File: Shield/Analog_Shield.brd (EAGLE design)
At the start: 115.2 x 89.7 mm, 74 parts, among them IC1 7805TV, IC2 LM340MP-05

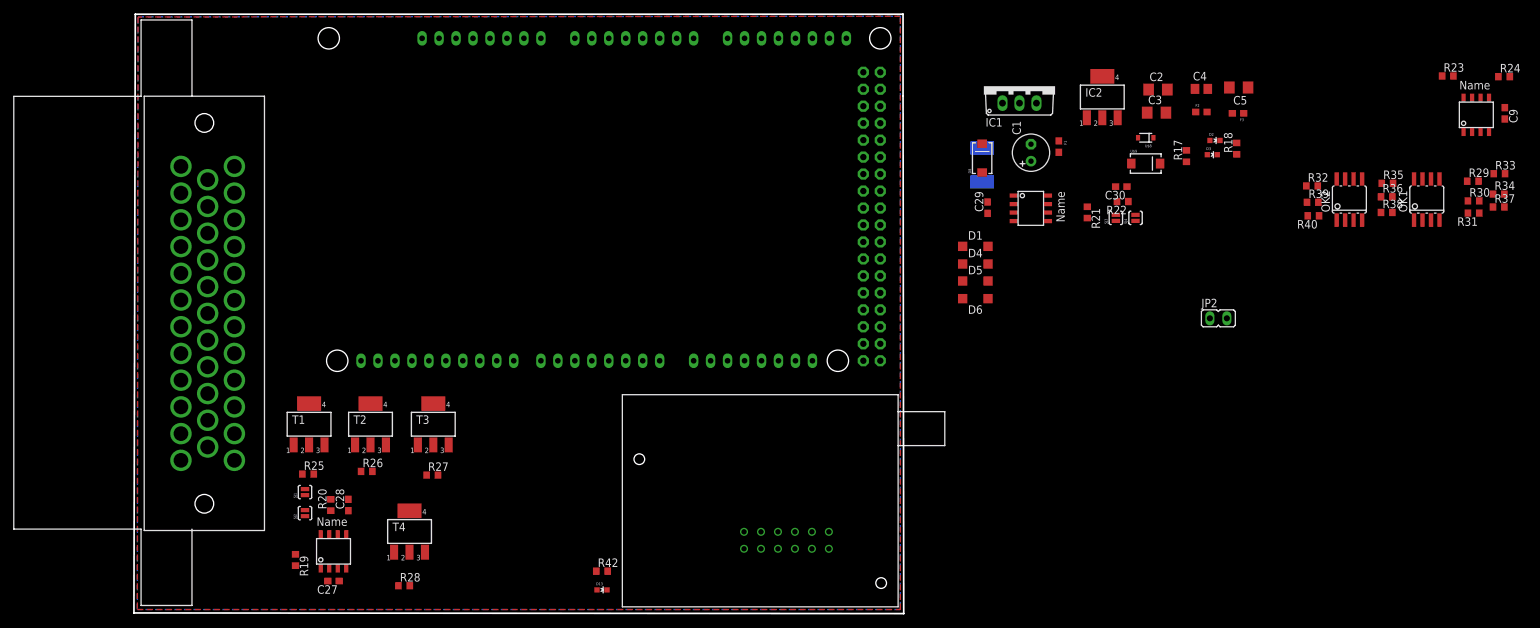
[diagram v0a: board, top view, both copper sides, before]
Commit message: Added analog shield, flipped Due on Dued board, fixed miniwifi footprint
Added an analog shield that will be used for all analog input instead of placing it on the main DueD board. Also, now all boards will be two layer instead of four.

Flipped over the Due on the DueD board. Now the DueD board is to have pins that stick up for the Due to
mate to.

Drastically improved the accuracy of the miniwifi layout.
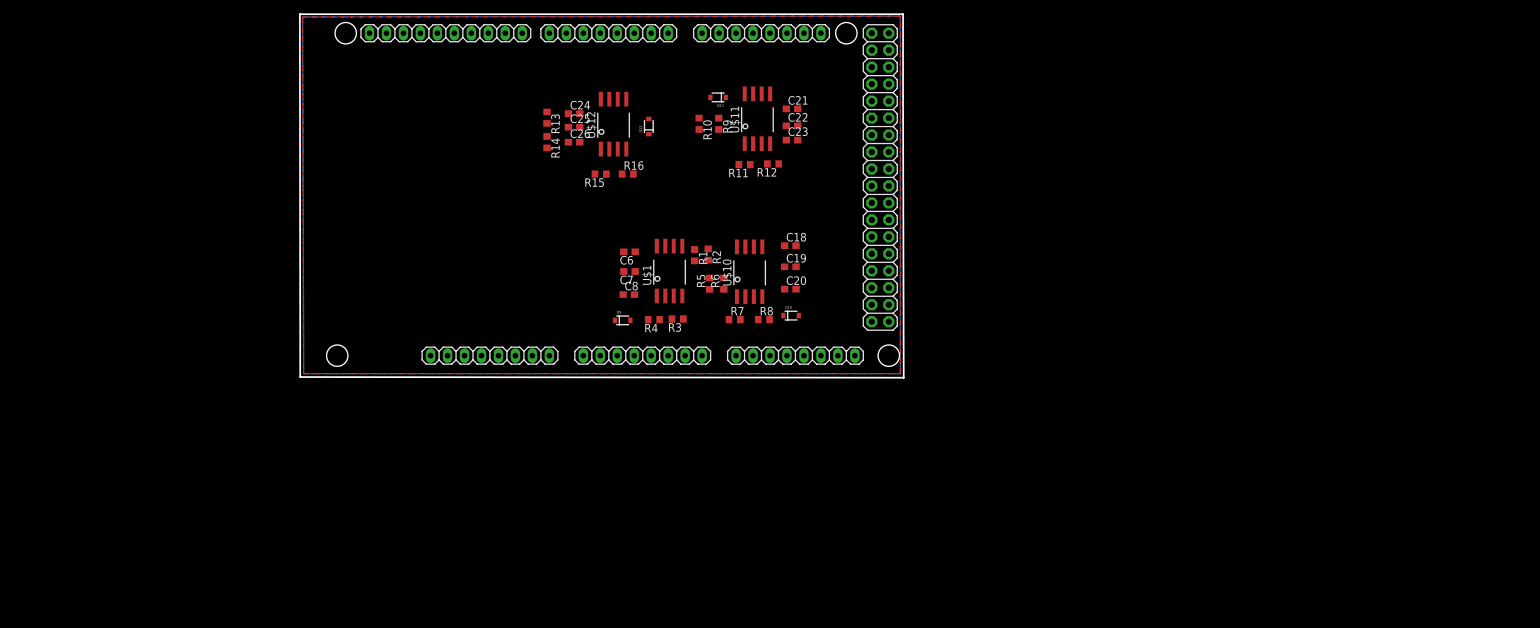
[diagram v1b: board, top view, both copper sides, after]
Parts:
- removed C1: 100uF, rcl:E2,5-6
- removed C2: 1uF, rcl:C1206
- removed C27, C29: .1uF, rcl:C0603
- removed C28, C30: 47nF, rcl:C0603
- removed C3: .1uF, rcl:C1206
- removed C4: .33uF, rcl:C0805
- removed C5: 10uF, rcl:C1206
- removed C9: (no value), rcl:C0603
- removed D1, D4, D5, D6: MBR0520LT, diode:SOD123
- removed D13, D2, D3: GREEN, SparkFun-LED:LED-0603
- removed D8: MBRA140, SparkFun-DiscreteSemi:SMA-DIODE
- removed F1, F2, F3: PTC0603, SparkFun-PowerIC:0603
- removed IC1: 7805TV, linear:TO220V
- removed IC2: LM340MP-05, linear:SOT223
- removed JP2: (no value), jumper:JP1
- removed L1: (no value), SparkFun-Passives:INDUCTOR-1206
- removed OK1, OK2: ILD213, optocoupler:SOIC08
- removed R17: 510, rcl:R0603
- removed R18: 330, rcl:R0603
- removed R19, R21, R25, R26, R27, R28, R31, R37, R38, R39: 10K, rcl:R0603
- removed R20, R22: 120, rcl:R0603
- removed R23, R24: 4.7K, rcl:R0603
- removed R29, R30, R32, R33, R34, R35, R36, R40: 1K, rcl:R0603
- removed R42: 33, rcl:R0603
- removed SJ1, SJ2, SJ3, SJ4: SOLDERJUMPERNO, SparkFun-Passives:SJ_2S-NO
- removed T1, T2, T3, T4: (no value), zetex:SOT223
- removed U$2, U$6: SN65HVD234, ck_custom:SOIC8
- removed U$3: AMPSEAL35, Ampseal:AMPSEAL35
- removed U$4: MINIWIFI, ck_custom:MINIWIFI
- removed U$5: M24M02-DRMN6TP, ck_custom:SOIC8
- removed U$8: DIODE-ZENER-BZT52, SparkFun-DiscreteSemi:SOD-323
- removed U$9: TVS, SparkFun-DiscreteSemi:SMA-DIODE
- added C18, C19, C21, C22, C24, C25, C6, C7: .1uF, rcl:C0603
- added C20, C23, C26, C8: 100pf, rcl:C0603
- added D10, D11, D12, D9: TVS, SparkFun-DiscreteSemi:SOD-323
- added R1, R10, R11, R13, R14, R15, R2, R3, R5, R6, R7, R9: 10K, rcl:R0603
- added R12, R16, R4, R8: 16K, rcl:R0603
- added U$1, U$10, U$11, U$12: ACPL-C87A-000E, ck_custom:SO8-WIDE
- moved COMMUNICATION 49.0 mm to (77.5, 50.8), flipped to the top, turned to 0 degrees
- moved PWMH 49.0 mm to (30.2, 50.8), flipped to the top, turned to 180 degrees
- moved PWML 49.0 mm to (54.6, 50.8), flipped to the top, turned to 180 degrees
- moved ADCH 47.5 mm to (82.5, 2.54), flipped to the top, turned to 0 degrees
- moved ADCL 47.5 mm to (59.7, 2.54), flipped to the top, turned to 0 degrees
- moved POWER 47.5 mm to (36.8, 2.54), flipped to the top, turned to 0 degrees
- moved XIO 5.98 mm to (95.2, 29.2), flipped to the top, turned to 270 degrees
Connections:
- removed net +12V: C1.+, C2.1, C3.1, F1.2, IC1.1, JP2.1, U$3.2
- removed net CANH0: SJ1.1, U$3.11, U$6.PIN7
- removed net CANH1: SJ3.1, U$2.PIN7, U$3.13
- removed net CANL0: SJ2.1, U$3.12, U$6.PIN6
- removed net CANL1: SJ4.1, U$2.PIN6, U$3.14
- removed net DGND: L1.P$1, U$3.19, U$3.26, U$3.31
- removed net DIN1: R29.1, U$3.32
- removed net DIN2: R33.1, U$3.33
- removed net DIN3: R32.1, U$3.34
- removed net DIN4: R36.1, U$3.35
- removed net MOSFET1: D1.C, T1.2, T1.4, U$3.15
- removed net MOSFET2: D4.C, T2.2, T2.4, U$3.16
- removed net MOSFET3: D5.C, T3.2, T3.4, U$3.17
- removed net MOSFET4: D6.C, T4.2, T4.4, U$3.18
- removed net N$2: U$4.P$5, U$4.P$7
- removed net N$23: D2.A, R17.2
- removed net N$24: R19.2, U$6.PIN8
- removed net N$25: D3.A, R18.2
- removed net N$26: C28.1, R20.1, SJ2.2
- removed net N$27: R20.2, SJ1.2
- removed net N$28: R21.2, U$2.PIN8
- removed net N$29: C30.1, R22.1, SJ4.2
- removed net N$3: D8.C, F1.1, U$8.1, U$9.C
- removed net N$30: R22.2, SJ3.2
- removed net N$31: OK1.1, R29.2
- removed net N$32: OK1.3, R33.2
- removed net N$33: OK1.8, R30.1
- removed net N$34: OK1.6, R34.1
- removed net N$36: OK2.6, R35.1
- removed net N$38: OK2.8, R40.1
- removed net N$4: R42.2, U$4.P$12
- removed net N$40: OK2.1, R32.2
- removed net N$43: OK2.3, R36.2
- removed net N$6: C4.1, F2.1, IC1.3
- removed net N$8: C5.1, F3.1, IC2.3
- removed net N$9: D13.A, R42.1
- removed net V_IN: D8.A, U$3.1
- new net N$10: R3.2, R4.1, U$1.2
- new net N$11: R7.2, R8.1, U$10.2
- new net N$12: R5.1, U$10.7
- new net N$13: R6.1, U$10.6
- new net N$15: R11.2, R12.1, U$11.2
- new net N$16: R9.1, U$11.7
- new net N$17: R10.1, U$11.6
- new net N$19: R15.2, R16.1, U$12.2
- new net N$20: R13.1, U$12.7
- new net N$21: R14.1, U$12.6
- new net N$5: R1.1, U$1.7
- new net N$7: R2.1, U$1.6
- net +3V3: no longer C27.1, C29.1, C9.1, F3.2, R18.1, R23.1, R24.1, R31.2, R37.2, R38.2, R39.2, U$2.PIN3, U$4.P$1, U$5.PIN8, U$6.PIN3
- net +5V: now also C18.1, C19.1, C21.1, C22.1, C24.1, C25.1, C6.1, C7.1, U$1.1, U$1.8, U$10.1, U$10.8, U$11.1, U$11.8, U$12.1, U$12.8; no longer F2.2, IC2.1, R17.1, U$3.3
- net AD0: now also R1.2
- net AD1: now also R2.2
- net AD2: now also R5.2
- net AD3: now also R6.2
- net AD4: now also R9.2
- net AD5: now also R10.2
- net AD6: now also R13.2
- net AD7: now also R14.2
- net AIN1: now also C8.1, D9.1, R4.2; no longer U$3.27
- net AIN2: now also C20.1, D10.1, R8.2; no longer U$3.28
- net AIN3: now also C23.1, D11.1, R12.2; no longer U$3.29
- net AIN4: now also C26.1, D12.1, R16.2; no longer U$3.30
- net CAN0-EN: no longer U$6.PIN5
- net CAN1-EN: no longer U$2.PIN5
- net CANRX0: no longer U$6.PIN4
- net CANRX1: no longer U$2.PIN4
- net CANTX0: no longer U$6.PIN1
- net CANTX1: no longer U$2.PIN1
- net DIG1: no longer R30.2, R31.1
- net DIG2: no longer R34.2, R37.1
- net DIG3: no longer R39.1, R40.2
- net DIG4: no longer R35.2, R38.1
- net DIGOUT1: no longer R25.1, T1.1
- net DIGOUT2: no longer R26.1, T2.1
- net DIGOUT3: no longer R27.1, T3.1
- net DIGOUT4: no longer R28.1, T4.1
- net GND: now also C18.2, C19.2, C20.2, C21.2, C22.2, C23.2, C24.2, C25.2, C26.2, C6.2, C7.2, C8.2, D10.2, D11.2, D12.2, D9.2, R11.1, R15.1, R3.1, R7.1, U$1.3, U$1.4, U$1.5, U$10.3, U$10.4, U$10.5, U$11.3, U$11.4, U$11.5, U$12.3, U$12.4, U$12.5; no longer C1.-, C2.2, C27.2, C28.2, C29.2, C3.2, C30.2, C4.2, C5.2, C9.2, D1.A, D13.C, D2.C, D3.C, D4.A, D5.A, D6.A, IC1.2, IC2.4, L1.P$2, OK1.2, OK1.4, OK1.5, OK1.7, OK2.2, OK2.4, OK2.5, OK2.7, R19.1, R21.1, R25.2, R26.2, R27.2, R28.2, T1.3, T2.3, T3.3, T4.3, U$2.PIN2, U$4.P$2, U$5.PIN1, U$5.PIN2, U$5.PIN3, U$5.PIN4, U$6.PIN2, U$8.2, U$9.A
- net RXD1: no longer U$5.PIN7
- net RXD2: no longer U$4.P$10
- net RXD3: no longer U$4.P$4
- net SCL: no longer R23.2, U$5.PIN6
- net SDA: no longer R24.2, U$5.PIN5
- net TXD3: no longer U$4.P$3
- net VIN: no longer JP2.2
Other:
- board size 115.2 x 89.7 mm -> 90.4 x 54.4 mm
